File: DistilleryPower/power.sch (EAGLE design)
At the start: 68 parts, among them IC1 SN65HVD230/1, IC2 MICROCHIP_BY_ELEMENT14_BATCH_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, IC4 ACS758LCB-050B-PFF-T, J1 GREEN-2P-5.0, J2 GREEN-2P-5.0, J3 GREEN-2P-5.0, J4 GREEN-2P-5.0, J5 GREEN-2P-5.0, Q1 BC807-16LT1SMD, T1 BT138-DSH, U1 STM32F042KXTX, X1 IQD-FREQUENCY-PRODUCTS_CRYSTA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, X2 2516-

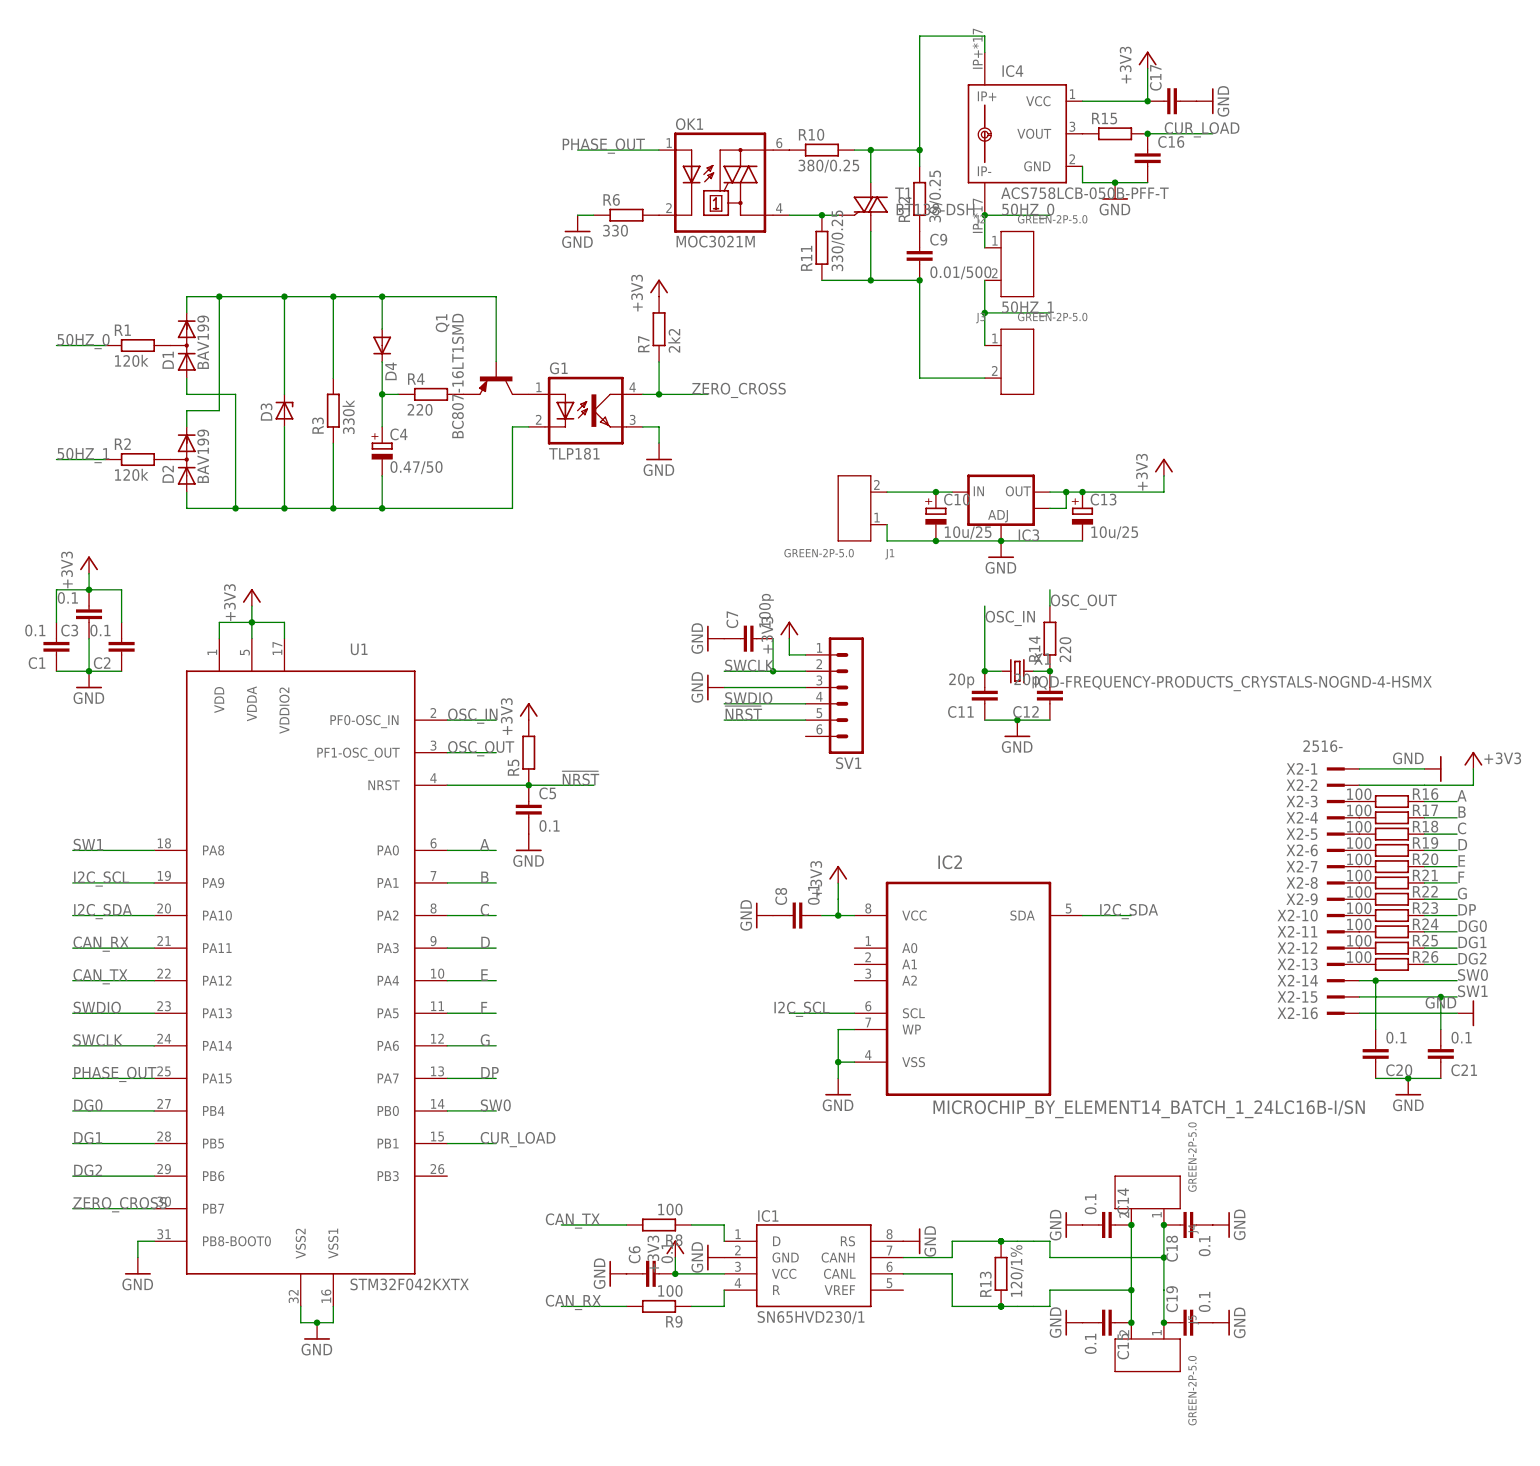
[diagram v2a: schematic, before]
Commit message: export all to local library; renumber symbols;
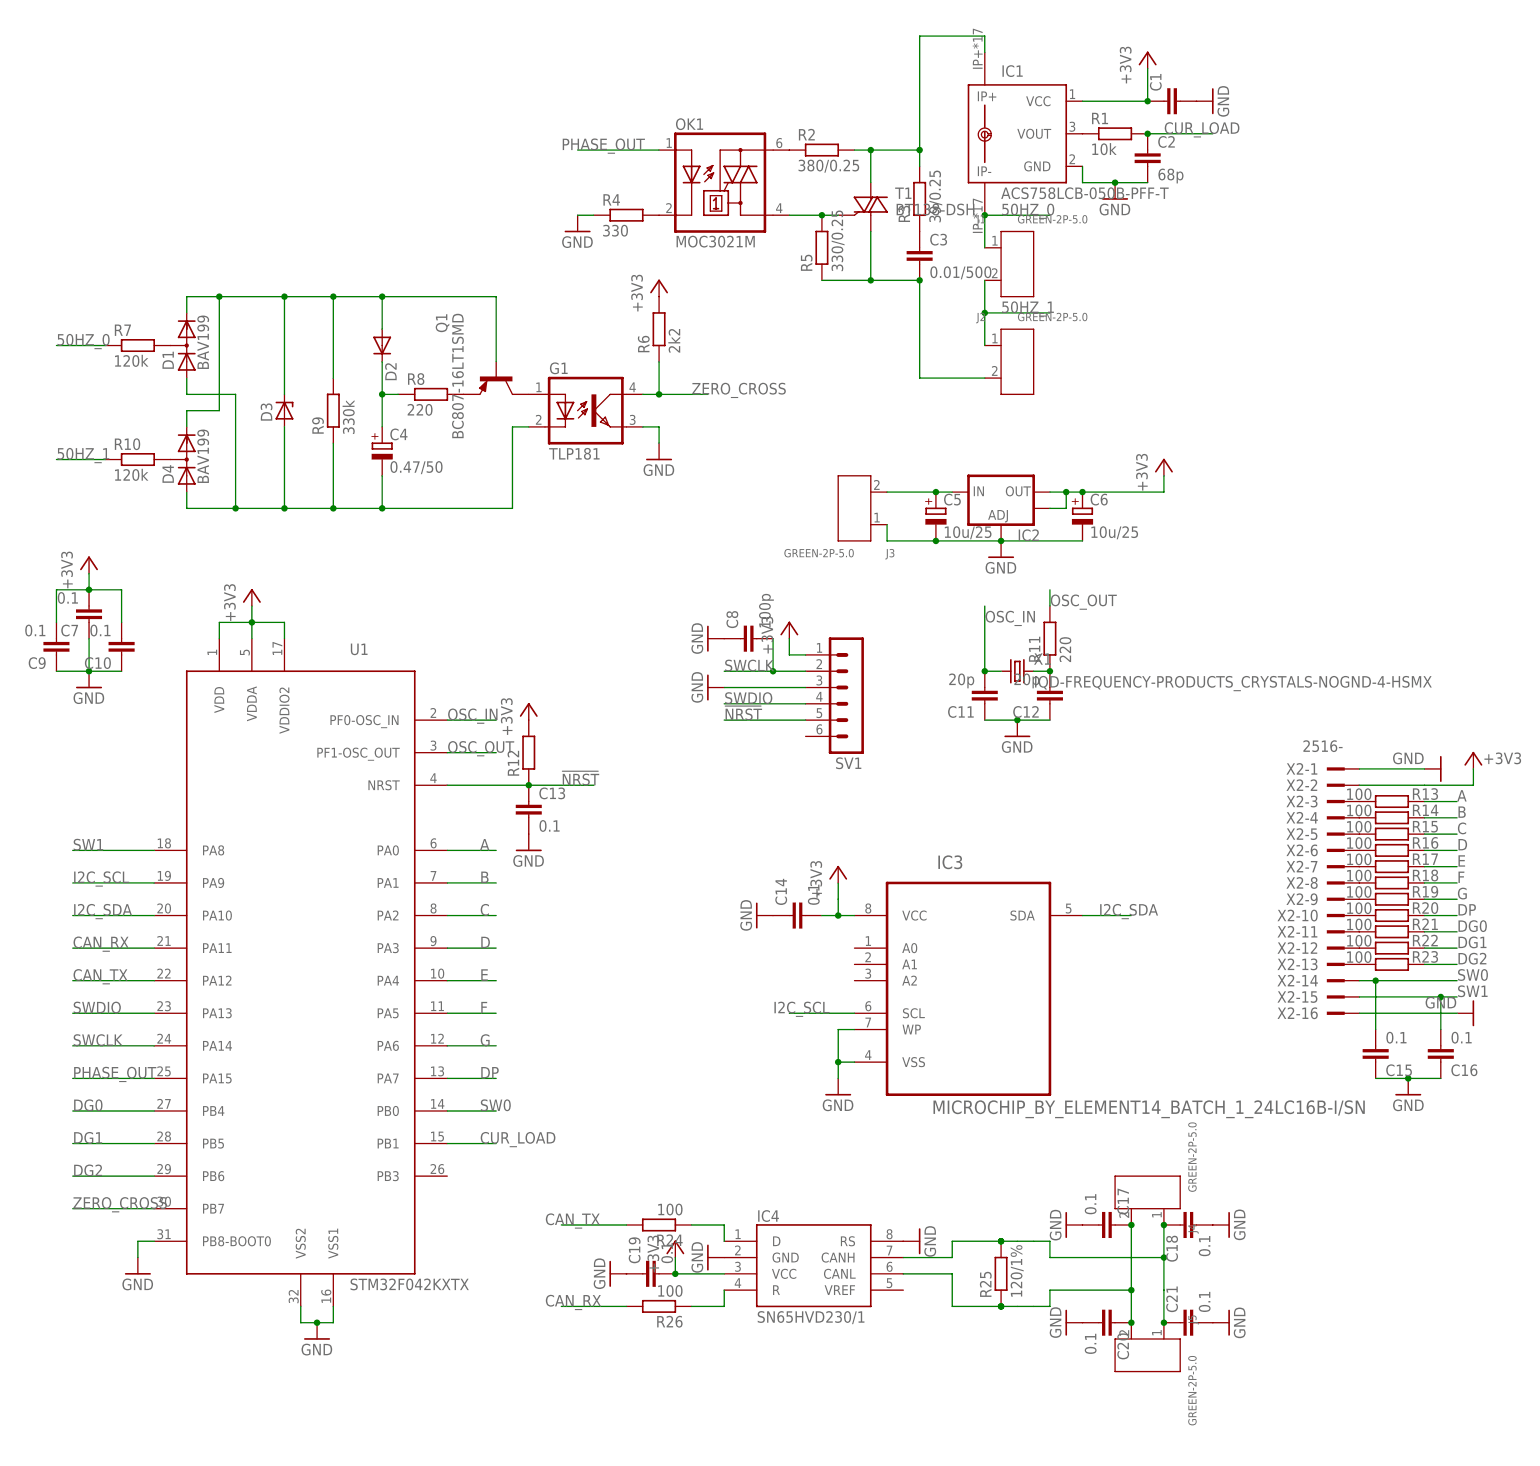
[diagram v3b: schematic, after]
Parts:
- C1: value 0.1 -> (none)
- C10, C13: value 10u/25 -> 0.1; device rcl:CPOL-EUSMCB -> rcl:C-EUC0603
- C16, C17: value (none) -> 0.1
- C2: value 0.1 -> 68p
- C3: value 0.1 -> 0.01/500; device rcl:C-EUC0603 -> rcl:C-EUC1206
- C5, C6: value 0.1 -> 10u/25; device rcl:C-EUC0603 -> rcl:CPOL-EUSMCB
- C7: value 100p -> 0.1
- C8: value 0.1 -> 100p
- C9: value 0.01/500 -> 0.1; device rcl:C-EUC1206 -> rcl:C-EUC0603
- D2: value BAV199 -> (none); device diode:BAV199 -> diode:DIODE-SOD523
- D4: value (none) -> BAV199; device diode:DIODE-SOD523 -> diode:BAV199
- IC1: value SN65HVD230/1 -> ACS758LCB-050B-PFF-T; device distillery:SN65HVD230/1 -> allegro:ACS758LCB-050B-PFF-T
- IC2: value MICROCHIP_BY_ELEMENT14_BATCH_1_24LC16B-I/SN -> (none); device distillery:MICROCHIP_BY_ELEMENT14_BATCH_1_24LC16B-I/SN -> SparkFun:V_REG_LM1117SOT223
- IC3: value (none) -> MICROCHIP_BY_ELEMENT14_BATCH_1_24LC16B-I/SN; device SparkFun:V_REG_LM1117SOT223 -> distillery:MICROCHIP_BY_ELEMENT14_BATCH_1_24LC16B-I/SN
- IC4: value ACS758LCB-050B-PFF-T -> SN65HVD230/1; device allegro:ACS758LCB-050B-PFF-T -> distillery:SN65HVD230/1
- R1: value 120k -> 10k; device rcl:R-EU_R1206 -> rcl:R-EU_R0603
- R10: value 380/0.25 -> 120k; device rcl:R-EU_M1206 -> rcl:R-EU_R1206
- R11: value 330/0.25 -> 220; device rcl:R-EU_M1206 -> rcl:R-EU_R0603
- R12: value 39/0.25 -> (none); device rcl:R-EU_M1206 -> rcl:R-EU_R0603
- R13: value 120/1% -> 100
- R14: value 220 -> 100
- R15: value (none) -> 100
- R2: value 120k -> 380/0.25; device rcl:R-EU_R1206 -> rcl:R-EU_M1206
- R25: value 100 -> 120/1%
- R3: value 330k -> 39/0.25; device rcl:R-EU_R1206 -> rcl:R-EU_M1206
- R4: value 220 -> 330; device rcl:R-EU_R1206 -> rcl:R-EU_R0603
- R5: value (none) -> 330/0.25; device rcl:R-EU_R0603 -> rcl:R-EU_M1206
- R6: value 330 -> 2k2
- R7: value 2k2 -> 120k; device rcl:R-EU_R0603 -> rcl:R-EU_R1206
- R8: value 100 -> 220; device rcl:R-EU_R0603 -> rcl:R-EU_R1206
- R9: value 100 -> 330k; device rcl:R-EU_R0603 -> rcl:R-EU_R1206
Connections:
- net !NRST: now also C13.1, R12.1; no longer C5.1, R5.1
- net +3V3: now also C1.1, C10.2, C14.2, C19.2, C6.+, C7.2, C9.2, IC2.OUT, IC2.OUT@1, IC3.VCC, R12.2, R6.2; no longer C1.2, C13.+, C17.1, C2.2, C3.2, C6.2, C8.2, IC2.VCC, IC3.OUT, IC3.OUT@1, R5.2, R7.2
- net 50HZ_0: now also IC1.IP-, J1.1, R7.1; no longer IC4.IP-, J2.1, R1.1
- net 50HZ_1: now also J1.2, J2.1, R10.1; no longer J2.2, J3.1, R2.1
- net A: now also R13.1; no longer R16.1
- net B: now also R14.1; no longer R17.1
- net C: now also R15.1; no longer R18.1
- net CAN_RX: now also R26.2; no longer R9.2
- net CAN_TX: now also R24.2; no longer R8.2
- net CUR_LOAD: now also C2.1, R1.2; no longer C16.1, R15.2
- net D: now also R16.1; no longer R19.1
- net DG0: now also R21.1; no longer R24.1
- net DG1: now also R22.1; no longer R25.1
- net DG2: now also R23.1; no longer R26.1
- net DP: now also R20.1; no longer R23.1
- net E: now also R17.1; no longer R20.1
- net F: now also R18.1; no longer R21.1
- net G: now also R19.1; no longer R22.1
- net GND: now also C1.2, C10.1, C13.2, C14.1, C15.1, C16.1, C19.1, C2.2, C20.2, C21.2, C5.-, C6.-, C9.1, IC2.ADJ, IC3.VSS, IC3.WP, IC4.RS, J3.1, R4.1; no longer C1.1, C10.-, C13.-, C14.2, C15.2, C16.2, C19.2, C2.1, C20.1, C21.1, C3.1, C5.2, C6.1, IC1.RS, IC2.VSS, IC2.WP, IC3.ADJ, J1.1, R6.1
- net I2C_SCL: now also IC3.SCL; no longer IC2.SCL
- net I2C_SDA: now also IC3.SDA; no longer IC2.SDA
- net N$1: now also R7.2; no longer R1.2
- net N$10: now also C3.1, R3.1; no longer C9.1, R12.1
- net N$11: now also R5.2; no longer R11.2
- net N$13: now also C5.+, IC2.IN, J3.2; no longer C10.+, IC3.IN, J1.2
- net N$14: now also R4.2; no longer R6.2
- net N$15: now also R13.2; no longer R16.2
- net N$16: now also R11.1; no longer R14.1
- net N$17: now also IC1.IP+, R2.2, R3.2; no longer IC4.IP+, R10.2, R12.2
- net N$18: now also C3.2, J2.2, R5.1; no longer C9.2, J3.2, R11.1
- net N$2: now also IC1.VOUT, R1.1; no longer IC4.VOUT, R15.1
- net N$20: now also C17.1, C20.1, IC4.CANL, R25.1; no longer C14.1, C15.1, IC1.CANL, R13.1
- net N$21: now also IC4.D, R24.1; no longer IC1.D, R8.1
- net N$22: now also IC4.R, R26.1; no longer IC1.R, R9.1
- net N$23: now also R14.2; no longer R17.2
- net N$24: now also C21.1, IC4.CANH, R25.2; no longer C19.1, IC1.CANH, R13.2
- net N$25: now also R15.2; no longer R18.2
- net N$26: now also R16.2; no longer R19.2
- net N$27: now also R17.2; no longer R20.2
- net N$28: now also R18.2; no longer R21.2
- net N$29: now also R19.2; no longer R22.2
- net N$3: now also D4.AC, R10.2; no longer D2.AC, R2.2
- net N$30: now also R20.2; no longer R23.2
- net N$31: now also R21.2; no longer R24.2
- net N$32: now also R22.2; no longer R25.2
- net N$33: now also R23.2; no longer R26.2
- net N$4: now also D2.A, D4.C, R9.2; no longer D2.C, D4.A, R3.2
- net N$5: now also D4.A, R9.1; no longer D2.A, R3.1
- net N$6: now also D2.C, R8.1; no longer D4.C, R4.1
- net N$7: now also R8.2; no longer R4.2
- net N$9: now also R2.1; no longer R10.1
- net OSC_OUT: now also R11.2; no longer R14.2
- net SW0: now also C15.2; no longer C20.2
- net SW1: now also C16.2; no longer C21.2
- net SWCLK: now also C8.2; no longer C7.2
- net ZERO_CROSS: now also R6.1; no longer R7.1
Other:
- moved on the sheet: C1, C14, C15, C16, C17, C19, C2, C20, C21, C3, C7, C8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

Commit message: reroute: indication board with CAN controller
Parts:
- added C22, C23, C24, C25, C26: 0.1, rcl:C-EUC0603
- added C28: 10u/25, rcl:CPOL-EUSMCB
- added D5, D6, D7: CHRONO_LED_8X1, chrono:CHRONO_LED_8X1
- added IC5: SN65HVD230/1, distillery:SN65HVD230/1
- added U2: STM32F042KXTX, stm32f0:STM32F042KXTX
- added X3: 22-23-2041, con-molex:22-23-2041
- R14: value 100 -> 120/1%
- R16, R19, R20, R21, R22, R23, R24, R26: value 100 -> (none)
- R25: value 120/1% -> (none)
- X2: value 2516- -> 22-23-2041; device con-3m:2516- -> con-molex:22-23-2041
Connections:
- removed net DG0: R21.1, U1.PB4
- removed net DG1: R22.1, U1.PB5
- removed net DG2: R23.1, U1.PB6
- removed net N$33: R23.2, X2-13.KL
- removed net SW0: C15.2, U1.PB0, X2-14.KL
- removed net SW1: C16.2, U1.PA8, X2-15.KL
- new net !I_NRST: C20.1, R16.1, U2.NRST
- new net I_3V3: C21.2, C22.2, C23.2, C24.2, C28.+, IC5.VCC, R16.2, U2.VDD, U2.VDDA, U2.VDDIO2, X3-4.S
- new net I_CAN_RX: R18.2, U2.PA11
- new net I_CAN_TX: R17.2, U2.PA12
- new net I_GND: C20.2, C21.1, C22.1, C23.1, C24.1, C25.2, C26.2, C28.-, IC5.GND, IC5.RS, U2.PB8-BOOT0, U2.VSS1, U2.VSS2, X3-1.S
- new net I_OSC_IN: U2.PF0-OSC_IN
- new net I_OSC_OUT: U2.PF1-OSC_OUT
- new net LED_1: D5.AN, D5.AN@1
- new net LED_2: D6.AN, D6.AN@1
- new net LED_3: D7.AN, D7.AN@1
- new net N$12: C25.1, IC5.CANL, X3-3.S
- new net N$19: IC5.R, R18.1
- net +3V3: now also C17.2, X2-4.S; no longer C19.2, X2-2.KL
- net A: now also D5.A, D6.A, D7.A, R19.1; no longer R13.1, U1.PA0
- net B: now also D5.B, D6.B, D7.B, R20.1; no longer R14.1, U1.PA1
- net C: now also D5.C, D6.C, D7.C, R21.1; no longer R15.1, U1.PA2
- net CAN_RX: now also R15.2; no longer R26.2
- net CAN_TX: now also R13.2; no longer R24.2
- net CUR_LOAD: now also U1.PA4; no longer U1.PB1
- net D: now also D5.D, D6.D, D7.D, R22.1; no longer R16.1, U1.PA3
- net DP: now also D5.DP, D6.DP, D7.DP, R26.1; no longer R20.1, U1.PA7
- net E: now also D5.E, D6.E, D7.E, R23.1; no longer R17.1, U1.PA4
- net F: now also D5.F, D6.F, D7.F, R24.1; no longer R18.1, U1.PA5
- net G: now also D5.G, D6.G, D7.G, R25.1; no longer R19.1, U1.PA6
- net GND: now also C15.2, C16.2, C17.1, C19.2, X2-1.S; no longer C15.1, C16.1, C17.2, C19.1, C20.2, C21.2, X2-1.KL, X2-16.KL
- net N$15: now also IC5.D, R17.1; no longer R13.2, X2-3.KL
- net N$20: now also C15.1, C18.1, R14.1, X2-3.S; no longer C17.1, C20.1, R25.1
- net N$21: now also R13.1; no longer R24.1
- net N$22: now also R15.1; no longer R26.1
- net N$23: now also C26.1, IC5.CANH, X3-2.S; no longer R14.2, X2-4.KL
- net N$24: now also C16.1, C19.1, R14.2, X2-2.S; no longer C18.1, C21.1, R25.2
- net N$25: now also R19.2, U2.PA0; no longer R15.2, X2-5.KL
- net N$26: now also R20.2, U2.PA1; no longer R16.2, X2-6.KL
- net N$27: now also R21.2, U2.PA2; no longer R17.2, X2-7.KL
- net N$28: now also R22.2, U2.PA3; no longer R18.2, X2-8.KL
- net N$29: now also R23.2, U2.PA4; no longer R19.2, X2-9.KL
- net N$30: now also R24.2, U2.PA5; no longer R20.2, X2-10.KL
- net N$31: now also R25.2, U2.PA6; no longer R21.2, X2-11.KL
- net N$32: now also R26.2, U2.PA7; no longer R22.2, X2-12.KL
- net PHASE_OUT: now also U1.PA3; no longer U1.PA15
- net ZERO_CROSS: now also U1.PA5; no longer U1.PB7
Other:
- moved on the sheet: C15, C16, C17, C18, C19, C20, C21, R13, R14, R15, R16, R17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

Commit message: indication board routing finished
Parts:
- added C27: 100p, rcl:C-EUC0603
- added C29, C30: 20p, rcl:C-EUC0603
- added R27, R28, R29: 10k, rcl:R-EU_R0603
- added R30: 220, rcl:R-EU_R0603
- added S1, S2: SWITCH-TACT_DTS-6, chrono:SWITCH-TACT_DTS-6
- added SV2: (no value), distillery:CON-LSTB_MA06-1
- added VT1, VT2, VT3: WALKGEEK-EAGLE_IRLML6402, chrono:WALKGEEK-EAGLE_IRLML6402
- added X4: IQD-FREQUENCY-PRODUCTS_CRYSTALS-NOGND-4-HSMX, distillery:IQD-FREQUENCY-PRODUCTS_CRYSTALS-NOGND-4-HSMX
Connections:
- removed net LED_1: D5.AN, D5.AN@1
- removed net LED_2: D6.AN, D6.AN@1
- removed net LED_3: D7.AN, D7.AN@1
- new net AN_LED_1: D5.AN@1, VT1.D
- new net AN_LED_2: D6.AN@1, VT2.D
- new net AN_LED_3: D7.AN@1, VT3.D
- new net BTN_1: S2.3, S2.4, U2.PA2
- new net BTN_2: S1.3, S1.4, U2.PA9
- new net I_SWCLK: C27.2, SV2.2, U2.PA14
- new net I_SWDIO: SV2.4, U2.PA13
- new net N$33: C30.2, R30.1, X4.2
- new net P_LED_1: R27.2, U2.PB5, VT1.G
- new net P_LED_2: R28.2, U2.PB6, VT2.G
- new net P_LED_3: R29.2, U2.PB7, VT3.G
- net !I_NRST: now also SV2.5
- net A: now also R21.1; no longer R19.1
- net B: now also R19.1; no longer R20.1
- net C: now also R25.1; no longer R21.1
- net DP: now also R23.1; no longer R26.1
- net E: now also R24.1; no longer R23.1
- net F: now also R20.1; no longer R24.1
- net G: now also R26.1; no longer R25.1
- net I_3V3: now also R27.1, R28.1, R29.1, SV2.1, VT1.S, VT2.S, VT3.S
- net I_GND: now also C27.1, C29.1, C30.1, S1.1, S1.2, S2.1, S2.2, SV2.3
- net I_OSC_IN: now also C29.2, X4.1
- net I_OSC_OUT: now also R30.2
- net N$25: now also U2.PB0; no longer U2.PA0
- net N$26: now also U2.PB1; no longer U2.PA1
- net N$27: now also U2.PA8; no longer U2.PA2
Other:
- moved on the sheet: R19, R20, R21
